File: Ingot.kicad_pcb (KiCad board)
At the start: 2 copper layers, 228.6 x 76.2 mm, 92 parts

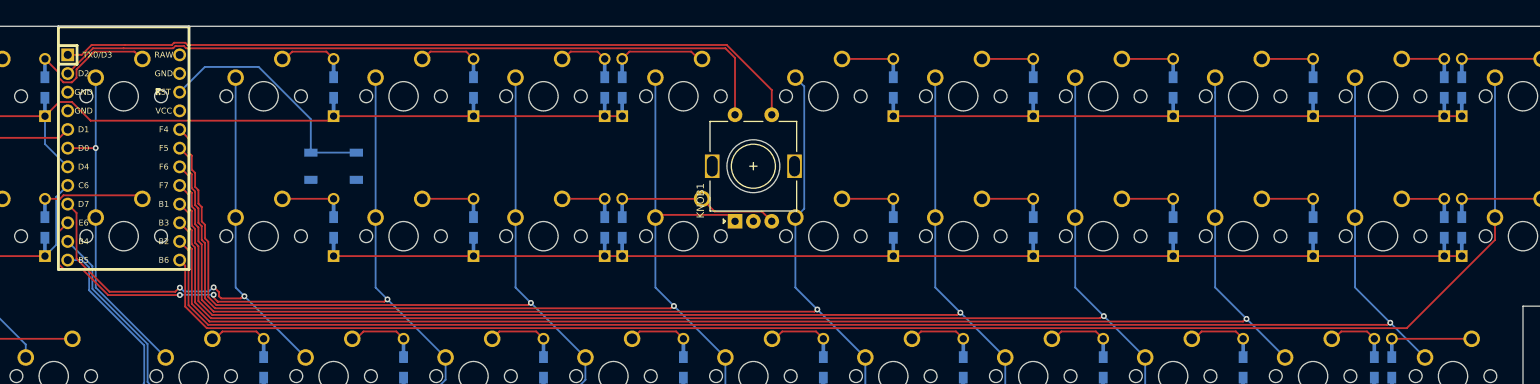
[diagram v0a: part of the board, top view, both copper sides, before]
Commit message: fixed a few ladybug issues
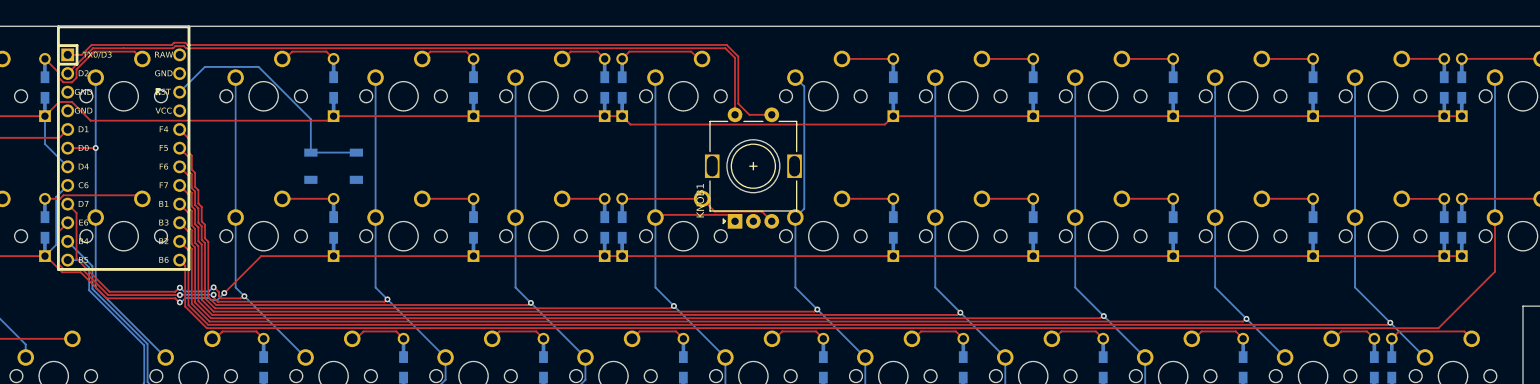
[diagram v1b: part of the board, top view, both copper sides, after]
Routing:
- net r2: track 181.2 -> 225.9 mm, vias 0 -> 2
- net r1: track 184.7 -> 222.6 mm
- net c12: track 213.2 -> 215.8 mm
- net X1: track 103.0 -> 104.8 mm
- net Net-(D35-Pad2): track 10.9 -> 11.7 mm
